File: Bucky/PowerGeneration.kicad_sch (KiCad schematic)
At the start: 47 parts, among them IC1201 MAX25262AFOF_VY+, IC801 TPS629206QDRLRQ1, Q801 PMV90ENER, Q802 PMV90ENER, U1 TPS2116DRLR, U802 LMR36506MSC5RPERQ1

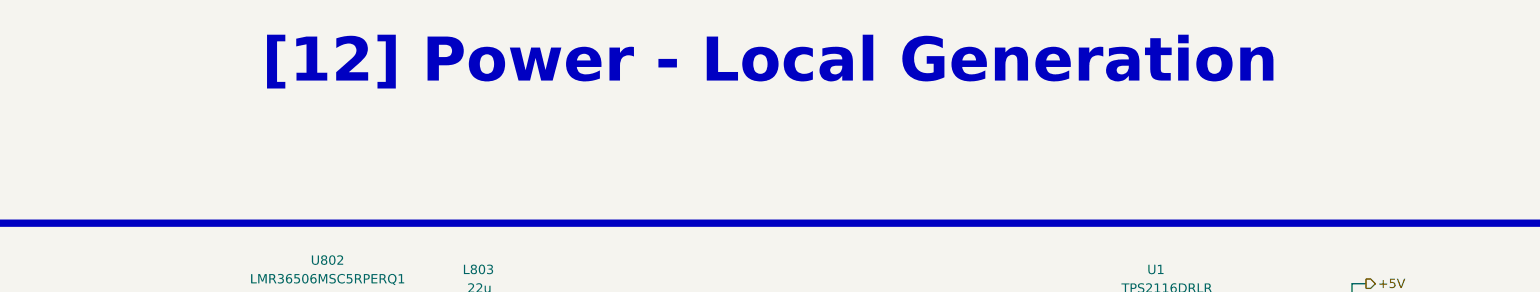
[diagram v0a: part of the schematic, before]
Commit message: adapted schematics and added more protection from GEODE (Reverse Current)
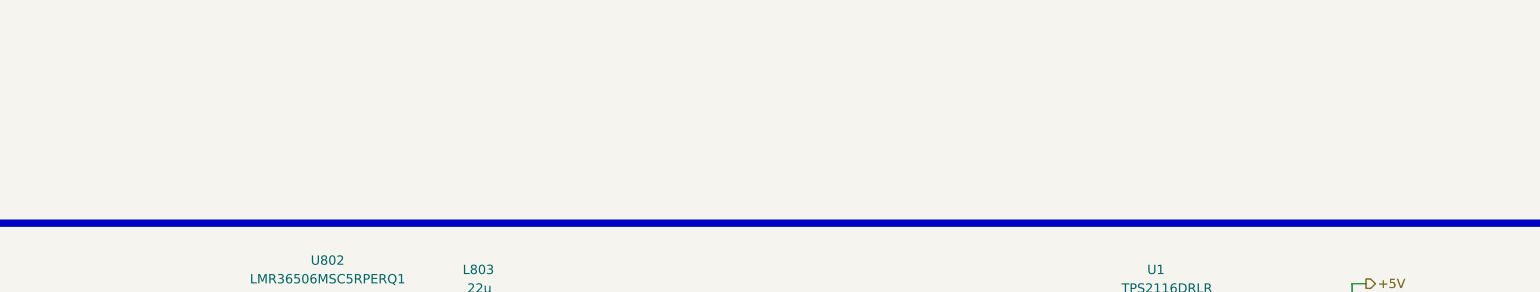
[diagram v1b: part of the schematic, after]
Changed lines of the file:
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@@
-		)
-	)
-	(text_box "[12] Power - Local Generation\n"
-		(exclude_from_sim no)
-		(at 17.145 14.605 0)
-		(size 394.97 12.7)
-		(margins 4.4999 4.4999 4.4999 4.4999)
-		(stroke
-			(width -0.0001)
-			(type default)
-		)
-		(fill
-			(type none)
-		)
-		(effects
-			(font
-				(face "Times New Roman")
-				(size 6 6)
-				(thickness 1.2)
-				(bold yes)
-				(color 162 22 34 1)
-			)
 		)
 	)

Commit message: upadated scchematics
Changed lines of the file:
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@@
+		)
+	)
+	(text_box "Local Power generation to power the MCU and peripherals. Schematics adapted from GEODE\n"
+		(exclude_from_sim no)
+		(at 49.53 171.45 0)
+		(size 53.34 19.05)
+		(margins 0.9525 0.9525 0.9525 0.9525)
+		(stroke
+			(width 0.0508)
+			(type solid)
+		)
+		(fill
+			(type none)
+		)
+		(effects
+			(font
+				(face "Arial")
+				(size 2.54 2.54)
+				(color 0 0 0 1)
+			)
+			(justify top)
 		)
 	)

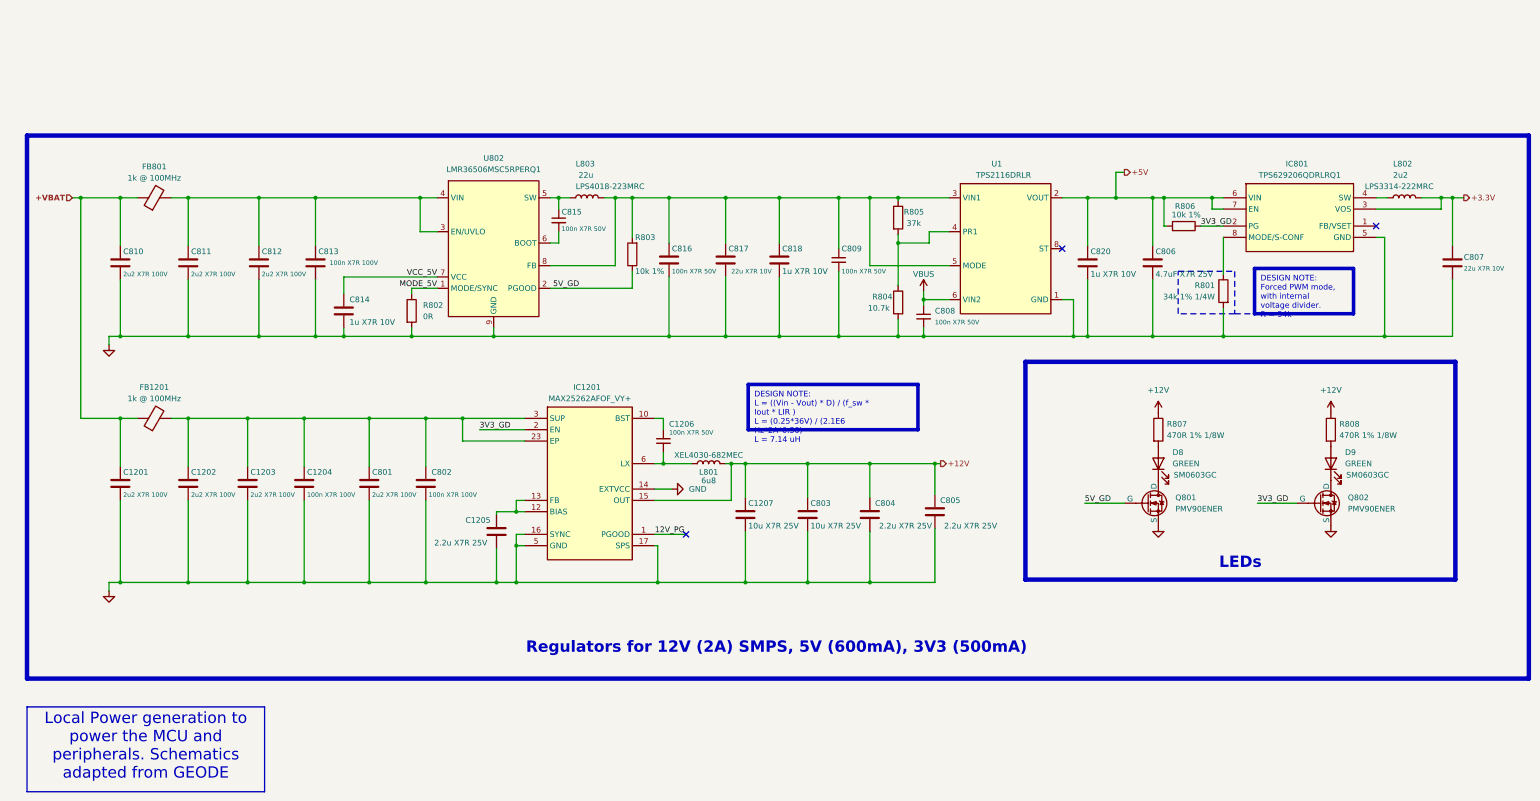
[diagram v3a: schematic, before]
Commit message: removed 12V local generation
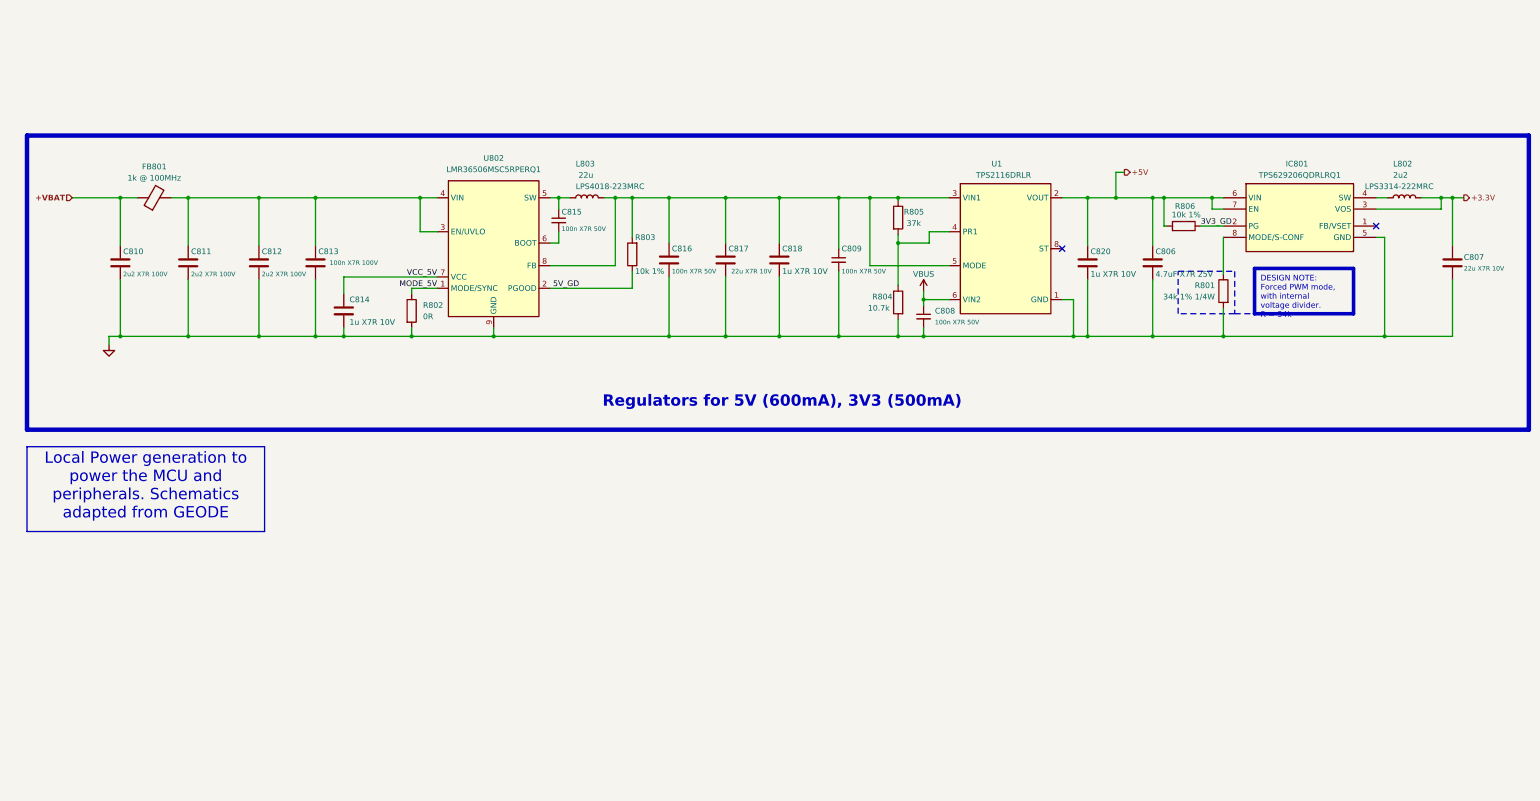
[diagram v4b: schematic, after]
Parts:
- removed C1201, C1202, C1203, C801: 2u2 X7R 100V, 0_capacitor_smd:C_0805_2012_DensityHigh, symbol Device:C
- removed C1204, C802: 100n X7R 100V, 0_capacitor_smd:C_0805_2012_DensityHigh, symbol Device:C
- removed C1205, C804, C805: 2.2u X7R 25V, 0_capacitor_smd:C_0805_2012_DensityHigh, symbol Device:C
- removed C1206: 100n X7R 50V, 0_capacitor_smd:C_0402_1005_DensityHigh, symbol Device:C_Small
- removed C1207, C803: 10u X7R 25V, 0_capacitor_smd:C_1210_3225_DensityHigh, symbol Device:C
- removed D8, D9: GREEN, LED_SMD:LED_0603_1608Metric, symbol Device:LED
- removed FB1201: 1k @ 100MHz, 0_resistor_smd:R_0805_2012_DensityHigh, symbol Device:FerriteBead
- removed IC1201: MAX25262AFOF_VY+, 0_switching_regulator:MAX25262AFOFVY, symbol MAX25262AFOF_VY+:MAX25262AFOF_VY+
- removed L801: 6u8, 0_inductor_smd:XEL4030682MEC, symbol Device:L
- removed Q801, Q802: PMV90ENER, 0_package_SOT_TO_SMD:SOT-23-3, symbol Simulation_SPICE:NMOS
- removed R807, R808: 470R 1% 1/8W, 0_resistor_smd:R_0402_1005_DensityHigh, symbol Device:R
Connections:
- no-connect marks 3 -> 2
